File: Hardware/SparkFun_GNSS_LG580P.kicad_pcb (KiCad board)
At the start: 4 copper layers, 50.8 x 43.2 mm, 161 parts, among them J1 USB_C_Receptacle, J10 Conn_01x06, J2 Conn_01x06, J3 SMA_Edge, J4 Qwiic_RA, J5 SMA_Edge, J6 Conn_01x09, J7 Qwiic_RA, J8 JST_Locking_4, J9 I2C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

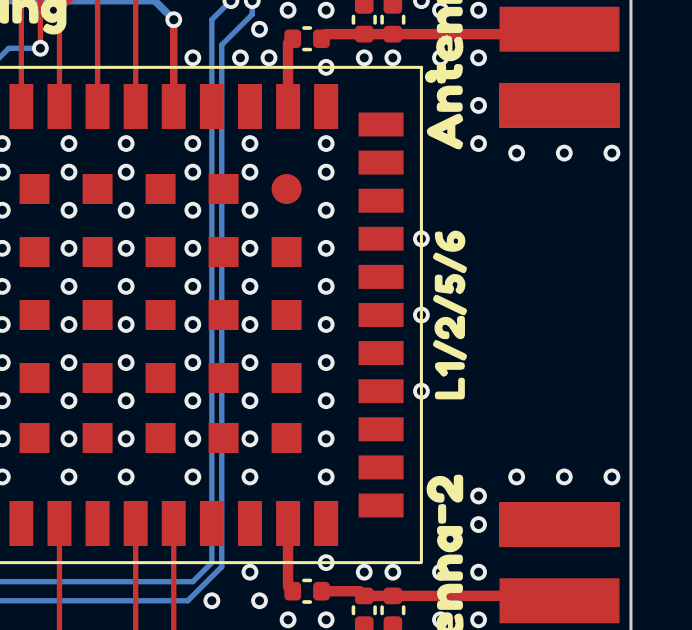
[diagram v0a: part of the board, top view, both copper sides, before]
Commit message: Adjust values for assembly
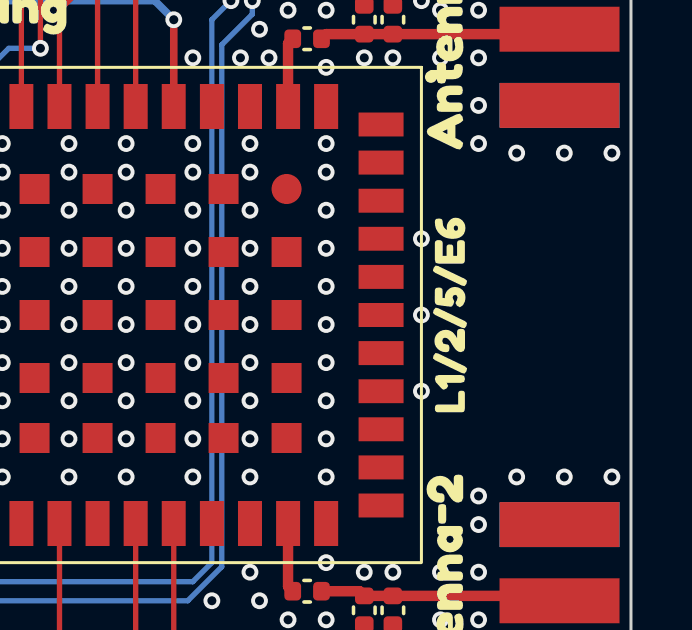
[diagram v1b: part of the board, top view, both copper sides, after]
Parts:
- removed kibuzzard-6797CEB8: G***, kibuzzard-6797CEB8
- added kibuzzard-67C8A377: G***, kibuzzard-67C8A377, F.Cu at (180.0, 95.9)

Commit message: Add panelized files
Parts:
- removed D6, D7: PESD0603-240, SparkFun-Capacitor:C_0603_1608Metric
- added D11: DF5A5.6LFU, SparkFun-Semiconductor-Standard:SOT-353, F.Cu at (155.9, 98.1)
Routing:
- net RXD1: track 18.5 -> 16.9 mm, vias 0 -> 2
- net 3.3V: track 40.1 -> 41.3 mm
- net TXD1: track 15.6 -> 14.7 mm
- net GND: track 7.09 -> 7.89 mm, vias 163 -> 165
- net V_BCKP: track 36.8 -> 37.6 mm
